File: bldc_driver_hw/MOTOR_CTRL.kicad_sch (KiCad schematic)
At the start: 0 parts

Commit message: wip
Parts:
- added C17: C_Snub, Capacitor_SMD:C_0805_2012Metric_Pad1.18x1.45mm_HandSolder, symbol Device:C_Small
- added C18: C_Small, Capacitor_SMD:C_0805_2012Metric_Pad1.18x1.45mm_HandSolder, symbol Device:C_Small
- added D2, D3, D5, D6: D_Schottky, symbol Device:D_Schottky
- added IC1: DRV8334PHPR, QFP50P900X900X120-49N, symbol bldc_driver_lib:DRV8334PHPR
- added Q1, Q2: NMOS, symbol Simulation_SPICE:NMOS
- added R11, R12, R14, R9: R_GATE, symbol Device:R_Small
- added R13, R15: R_GS, symbol Device:R_Small
- added R4: SHUNT, symbol Device:R_Small
- added R7: R_snub, symbol Device:R_Small
- added R8: C_snub, symbol Device:R_Small
- added TP2, TP3: TestPoint, symbol Connector:TestPoint
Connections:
- new net: D6.1 (K), R9.1
- new net: Q2.2 (G), R13.2, R14.2, R9.2, TP3.1
- new net: D6.2 (A), R14.1
- new net: C17.2, R7.1
- new net: Q1.2 (G), R11.2, R12.2, R15.2, TP2.1
- new net: D2.2 (A), Q2.3 (S), R13.1, R4.1
- new net: D5.1 (K), R11.1
- new net: D5.2 (A), R12.1
- new net: C18.2, R8.1
- new net +48V: D3.1 (K), Q1.1 (D), R8.2
- new net GND: R4.2, R7.2
- new net PHASE_A: C17.1, C18.1, D2.1 (K), D3.2 (A), Q1.3 (S), Q2.1 (D), R15.1

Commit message: wip
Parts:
- removed C17: C_Snub, Capacitor_SMD:C_0805_2012Metric_Pad1.18x1.45mm_HandSolder, symbol Device:C_Small
- removed C18: C_Small, Capacitor_SMD:C_0805_2012Metric_Pad1.18x1.45mm_HandSolder, symbol Device:C_Small
- removed D2, D3, D5, D6: D_Schottky, symbol Device:D_Schottky
- removed IC1: DRV8334PHPR, QFP50P900X900X120-49N, symbol bldc_driver_lib:DRV8334PHPR
- removed Q1, Q2: NMOS, symbol Simulation_SPICE:NMOS
- removed R11, R12, R14, R9: R_GATE, symbol Device:R_Small
- removed R13: R_GS, symbol Device:R_Small
- removed R4: SHUNT, symbol Device:R_Small
- removed R7: R_snub, symbol Device:R_Small
- removed R8: C_snub, symbol Device:R_Small
- removed TP2, TP3: TestPoint, symbol Connector:TestPoint
- added C21, C41, C42, C43, C53: 1uF, Capacitor_SMD:C_0805_2012Metric, symbol Device:C_Small
- added C38, C39: 470uF, symbol Device:C_Polarized_Small
- added C52: 100nF, Capacitor_SMD:C_0805_2012Metric, symbol Device:C_Small
- added C54: 47uF, symbol Device:C_Polarized_Small
- added C55: 10uF, Capacitor_SMD:C_0805_2012Metric, symbol Device:C_Small
- added R16: 100k, symbol Device:R_Small
- added R17: R_Small, symbol Device:R_Small
- added R23: 10k, symbol Device:R_Small
- added U3: DRV8328BRUYR, bldc_driver_footprint:QFN40P400X400X80-29N-D, symbol bldc_driver_lib:DRV8328BRUYR
- R15: value R_GS -> R_Small; now not fitted
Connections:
- net +48V: now also C38.1, C39.1, C52.2, C53.2, C54.1, U3.1 (PVDD)
- net GND: now also R15.2, C38.2, C39.2, C52.1, C53.1, C54.2, C55.2, R17.2, U3.17 (LSS), U3.28 (GND), U3.29 (EP)
- net PHASE_A: no longer names the net of R15.1
- net PHASE_A: now also U3.27 (DT)
- new net: R16.2, R17.1, U3.26 (VDSLVL)
- new net: C21.1, U3.3 (CPH)
- new net: C21.2, U3.2 (CPL)
- new net: C42.1, U3.9 (BSTB)
- new net: C41.1, U3.13 (BSTC)
- new net: C43.1, U3.5 (BSTA)
- new net +3.3V: R23.1
- new net H_PHASE_U/G_IN_H: U3.7 (GHA)
- new net H_PHASE_U/G_IN_L: U3.8 (GLA)
- new net H_PHASE_U/SRC_H: C43.2, U3.6 (SHA)
- new net H_PHASE_V/G_IN_H: U3.15 (GHC)
- new net H_PHASE_V/G_IN_L: U3.16 (GLC)
- new net H_PHASE_V/SRC_H: C41.2, U3.14 (SHC)
- new net H_PHASE_W/G_IN_H: U3.11 (GHB)
- new net H_PHASE_W/G_IN_L: U3.12 (GLB)
- new net H_PHASE_W/SRC_H: C42.2, U3.10 (SHB)
- new net IN_H_U: U3.23 (INLA)
- new net IN_H_V: U3.18 (INHC)
- new net IN_H_W: U3.19 (INHB)
- new net IN_L_U: U3.20 (INHA)
- new net IN_L_V: U3.21 (INLC)
- new net IN_L_W: U3.22 (INLB)
- new net IRQ_FAIL: R23.2, U3.24 (NFAULT)
- new net VGDD: C55.1, R16.1, U3.4 (GVDD)
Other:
- added sheet CSA (CSA.kicad_sch)
- added sheet CSA1 (CSA.kicad_sch)
- added sheet CSA2 (CSA.kicad_sch)
- added sheet H_PHASE_U (H_BRIDGE.kicad_sch)
- added sheet H_PHASE_V (H_BRIDGE.kicad_sch)
- added sheet H_PHASE_W (H_BRIDGE.kicad_sch)
- note added: "12A"
- note added: "30-40kHz"
- note added: "BULK CAPS"

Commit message: wip
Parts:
- removed C41, C42: 1uF, Capacitor_SMD:C_0805_2012Metric, symbol Device:C_Small
- added C78, C79: 1uF, Capacitor_SMD:C_0603_1608Metric_Pad1.08x0.95mm_HandSolder, symbol Device:C_Small
- added R25: 10k, Resistor_SMD:R_0603_1608Metric, symbol Device:R_Small
- added R63: 100k, Resistor_SMD:R_0805_2012Metric, symbol Device:R_Small
- added TH1: 10k, Resistor_SMD:R_0603_1608Metric, symbol Device:Thermistor_NTC
- C38, C39: footprint (none) -> Capacitor_THT:CP_Radial_D16.0mm_P7.50mm
- C43: footprint Capacitor_SMD:C_0805_2012Metric -> Capacitor_SMD:C_0603_1608Metric_Pad1.08x0.95mm_HandSolder; Rating 100V -> 50V
- C54: footprint (none) -> Capacitor_THT:CP_Radial_D10.0mm_P5.00mm
- C55: footprint Capacitor_SMD:C_0805_2012Metric -> Capacitor_SMD:C_0603_1608Metric
- R15, R16, R17, R23: footprint (none) -> Resistor_SMD:R_0603_1608Metric
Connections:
- net +3.3V: now also R25.1, TH1.1
- net GND: now also R63.1
- net H_PHASE_V/SRC_H: now also C79.2
- net H_PHASE_W/SRC_H: now also C78.2
- net at U3.9 (BSTB): now also C78.1
- net at U3.13 (BSTC): now also C79.1
- net at U3.25 (NSLEEP): now also R25.2
- new net TEMP_SENSOR: R63.2, TH1.2
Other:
- note removed: "12A"
- note removed: "30-40kHz"
- note removed: "BULK CAPS"
- moved on the sheet: R16, R17, R23

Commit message: schematic finished pcb in progress
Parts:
- added J11: Conn_01x02, Connector_AMASS:AMASS_XT60-F_1x02_P7.20mm_Vertical, symbol Connector_Generic:Conn_01x02
- added R24: 10k, Resistor_SMD:R_0805_2012Metric, symbol Device:R_Small
- added TH2: 10k, Resistor_SMD:R_0603_1608Metric, symbol Device:Thermistor_NTC
- added TP15, TP16, TP17, TP18, TP19, TP20, TP21, TP22, TP23, TP24, TP25: TestPoint, TestPoint:TestPoint_Pad_D2.0mm, symbol Connector:TestPoint
- C41: renamed from C21; footprint Capacitor_SMD:C_0805_2012Metric -> Capacitor_SMD:C_0603_1608Metric
- C45: renamed from C43; footprint Capacitor_SMD:C_0603_1608Metric_Pad1.08x0.95mm_HandSolder -> Capacitor_SMD:C_0603_1608Metric
- C46: renamed from C78; footprint Capacitor_SMD:C_0603_1608Metric_Pad1.08x0.95mm_HandSolder -> Capacitor_SMD:C_0603_1608Metric
- C47: renamed from C79; footprint Capacitor_SMD:C_0603_1608Metric_Pad1.08x0.95mm_HandSolder -> Capacitor_SMD:C_0603_1608Metric
- R23: renamed from R63; value 100k -> 10k
- renumbered C38 to C39, C39 to C40, C55 to C42, C52 to C43, C53 to C44, C54 to C48, R23 to R18, R16 to R19, R17 to R20, R15 to R21, R25 to R22, U3 to U7
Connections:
- net +3.3V: now also TH2.1
- net +48V: now also J11.1 (Pin_1), TP22.1
- net CURR_U: now also TP23.1
- net CURR_V: now also TP25.1
- net CURR_W: now also TP24.1
- net GND: now also J11.2 (Pin_2), R24.1
- net IN_H_U: now also TP20.1
- net IN_H_V: now also TP18.1
- net IN_H_W: now also TP16.1
- net IN_L_U: now also TP19.1
- net IN_L_V: now also TP17.1
- net IN_L_W: now also TP15.1
- net VGDD: now also TP21.1
- net TEMP_SENSOR renamed TEMP_SENSOR1
- new net TEMP_SENSOR2: R24.2, TH2.2
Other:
- moved on the sheet: C42, R22, R23, TH1

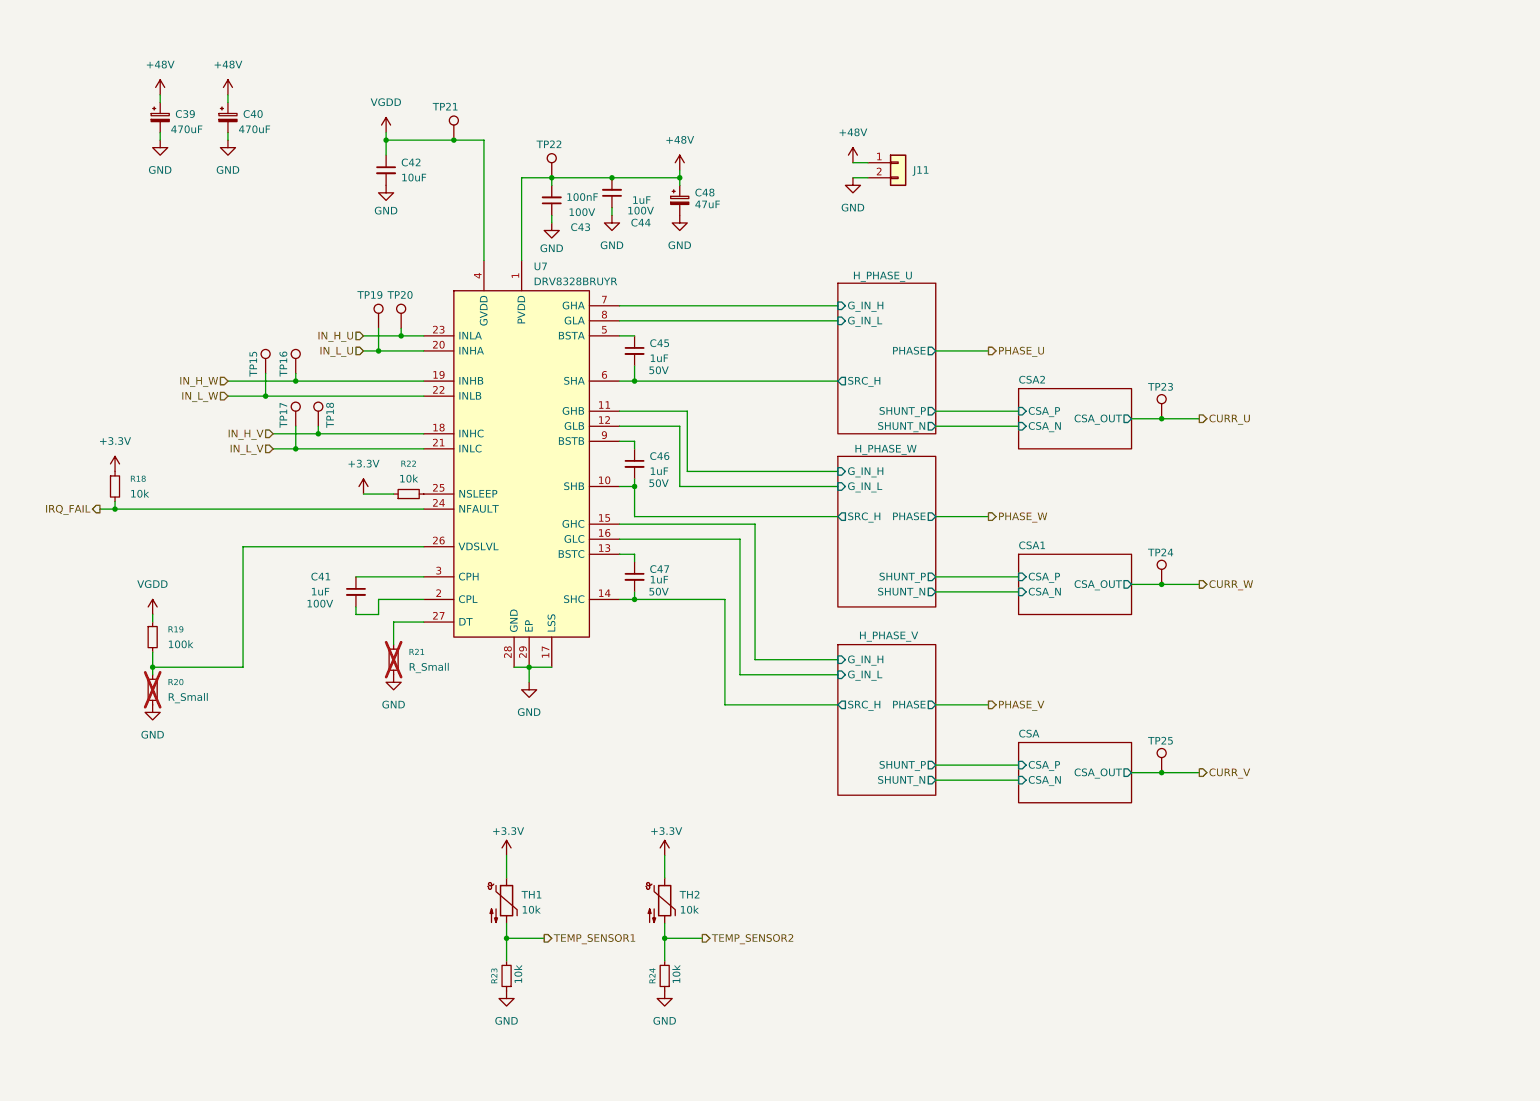
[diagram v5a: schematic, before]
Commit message: Changed one 3 phase driver to three h-bridges and changed buck converter which sink more current
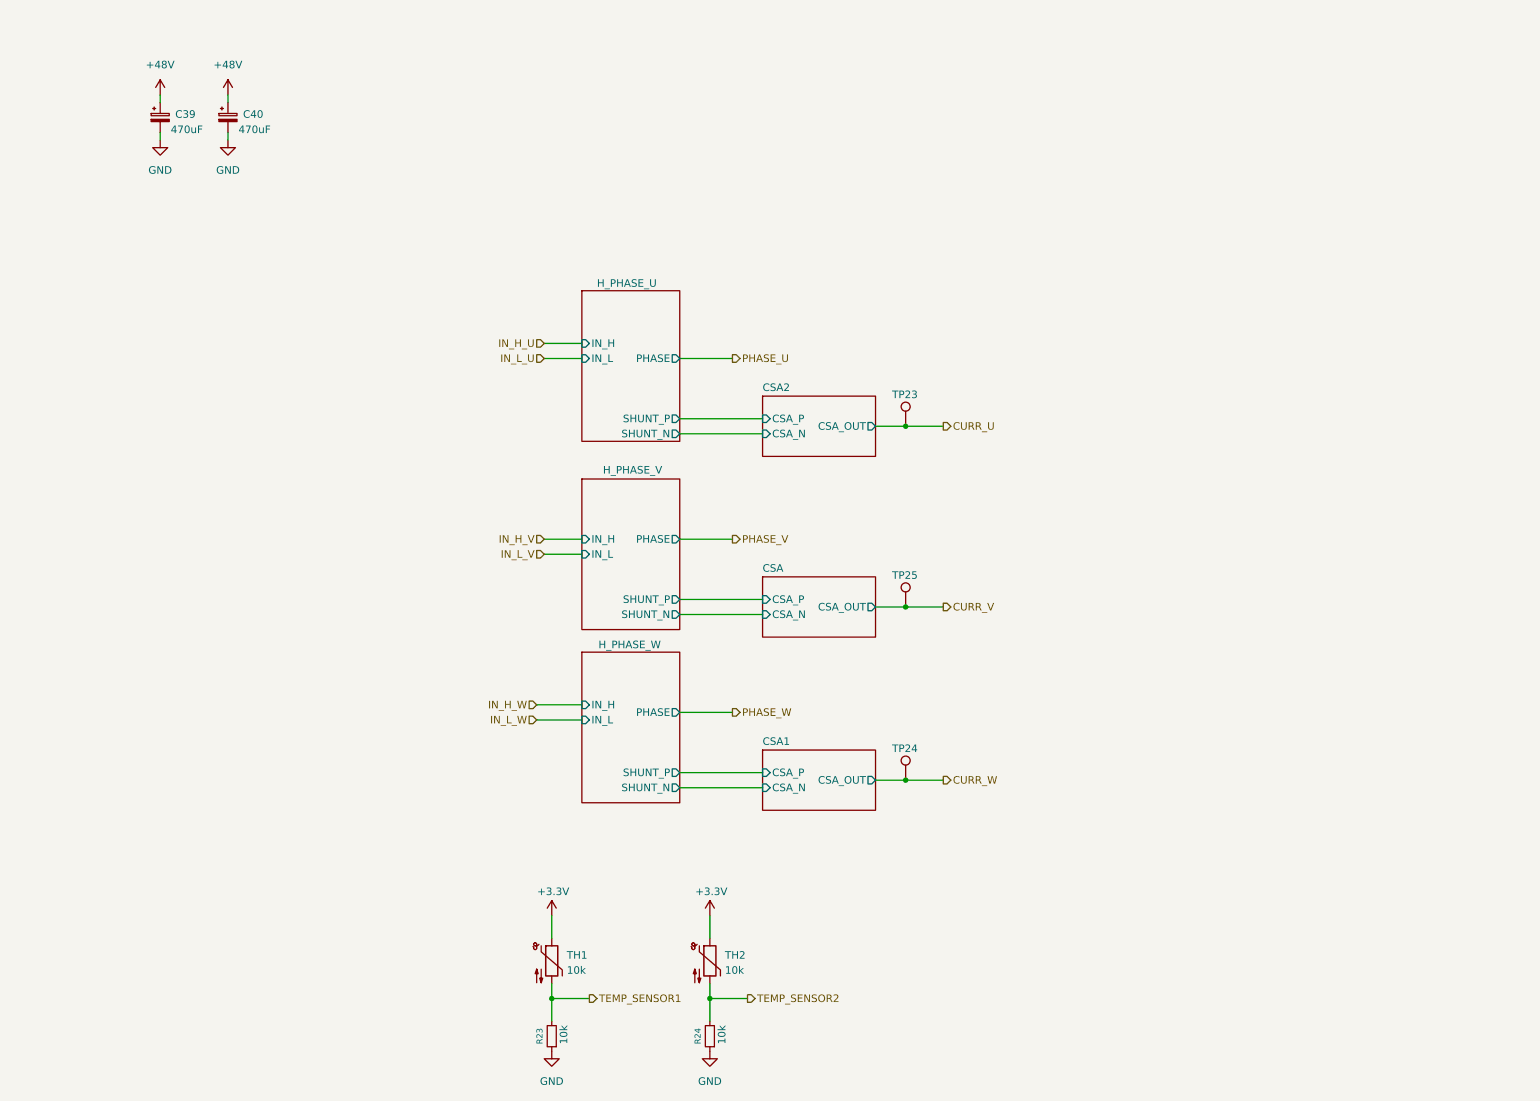
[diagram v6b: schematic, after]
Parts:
- removed C41, C45, C46, C47: 1uF, Capacitor_SMD:C_0603_1608Metric, symbol Device:C_Small
- removed C42: 10uF, Capacitor_SMD:C_0603_1608Metric, symbol Device:C_Small
- removed C43: 100nF, Capacitor_SMD:C_0805_2012Metric, symbol Device:C_Small
- removed C44: 1uF, Capacitor_SMD:C_0805_2012Metric, symbol Device:C_Small
- removed C48: 47uF, Capacitor_THT:CP_Radial_D10.0mm_P5.00mm, symbol Device:C_Polarized_Small
- removed J11: Conn_01x02, Connector_AMASS:AMASS_XT60-F_1x02_P7.20mm_Vertical, symbol Connector_Generic:Conn_01x02
- removed R18, R22: 10k, Resistor_SMD:R_0603_1608Metric, symbol Device:R_Small
- removed R19: 100k, Resistor_SMD:R_0603_1608Metric, symbol Device:R_Small
- removed R20, R21: R_Small, Resistor_SMD:R_0603_1608Metric, symbol Device:R_Small
- removed TP15, TP16, TP17, TP18, TP19, TP20, TP21, TP22: TestPoint, TestPoint:TestPoint_Pad_D2.0mm, symbol Connector:TestPoint
- removed U7: DRV8328BRUYR, bldc_driver_footprint:QFN40P400X400X80-29N-D, symbol bldc_driver_lib:DRV8328BRUYR
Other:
- sheet H_PHASE_U ports: added IN_H, IN_L; removed G_IN_H, G_IN_L, SRC_H
- sheet H_PHASE_V ports: added IN_H, IN_L; removed G_IN_H, G_IN_L, SRC_H
- sheet H_PHASE_W ports: added IN_H, IN_L; removed G_IN_H, G_IN_L, SRC_H
- moved on the sheet: R23, R24, TH1, TH2, TP23, TP24, TP25

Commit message: Board finished to review
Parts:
- added C41: 470uF, Capacitor_THT:CP_Radial_D16.0mm_P7.50mm, symbol Device:C_Polarized_Small
- added C45: 47uF, Capacitor_SMD:CP_Elec_6.3x5.4, symbol Device:C_Polarized_Small
- R23, R24: footprint Resistor_SMD:R_0805_2012Metric -> Resistor_SMD:R_0603_1608Metric
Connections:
- net +48V: now also C41.1
- net GND: now also C41.2, C45.2
- new net +12V: C45.1

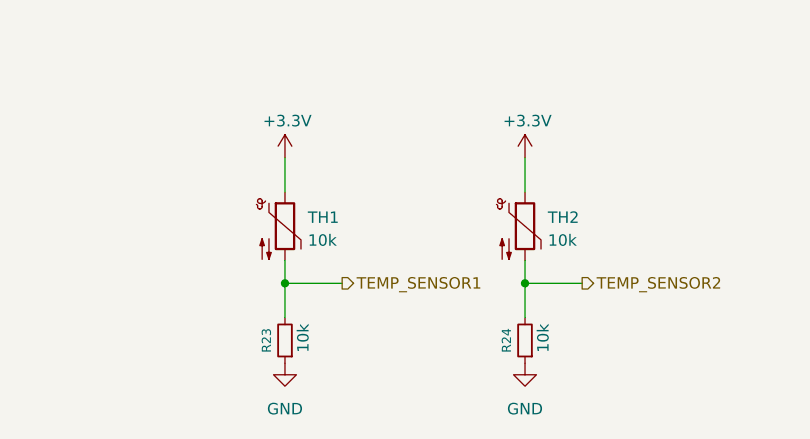
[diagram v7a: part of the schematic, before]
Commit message: added lcsc codes
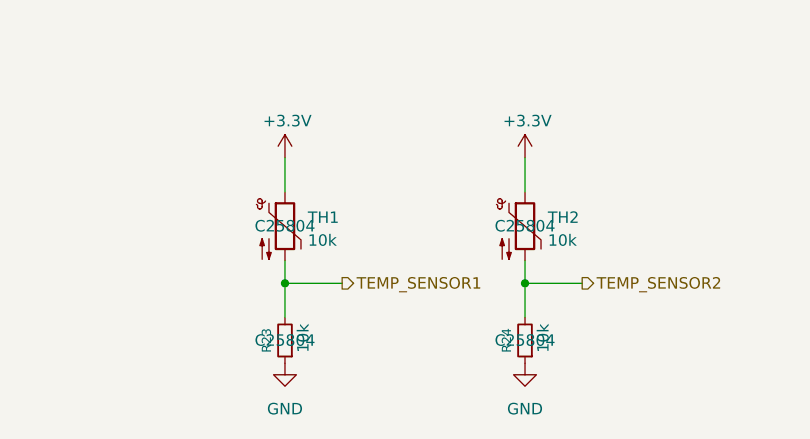
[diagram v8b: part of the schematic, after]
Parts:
- R23, R24, TH1, TH2: LCSC (none) -> C25804
